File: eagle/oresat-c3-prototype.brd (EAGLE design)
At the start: 99.8 x 94.7 mm, 107 parts, among them J1 J-SAMTEC-TFM-110-X1-XXX-D-RA, J10 2X8X1.27, J11 2X8X1.27, J12 2X8X1.27, J2 U.FL, J3 U.FL, J4 U.FL, J6 J-SAMTEC-TFM-120-X1-XXX-D-RA, J7 FTSH-105-XX-X-DV-K, J8 SD_CARD_SOCKET, J9 2X8X1.27, Q1 MOSFET-PCH-SOT23-6, U1 MAX892LEUA+T, U2 TCAN330, U3 TCAN330, U4 TPS259621 - eFuse, U5 TPS62111RSA, U6 MAX6373KA+21-0078H-L, U7 STM32F446RE, X1 16MHZ-2.5x2mm

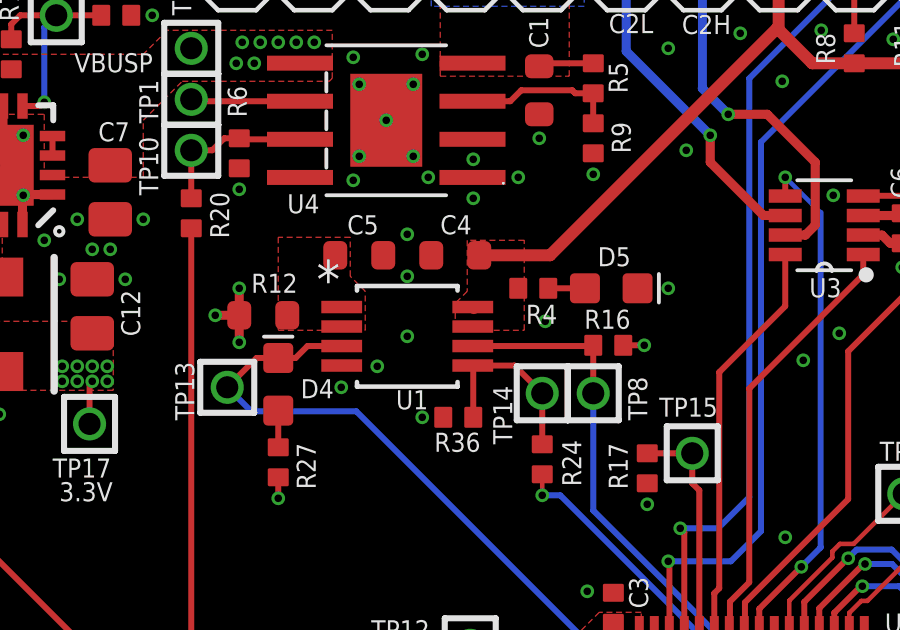
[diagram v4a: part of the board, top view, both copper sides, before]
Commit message: Replaced new ICs with versions in the oresat-eagle-libraries repo
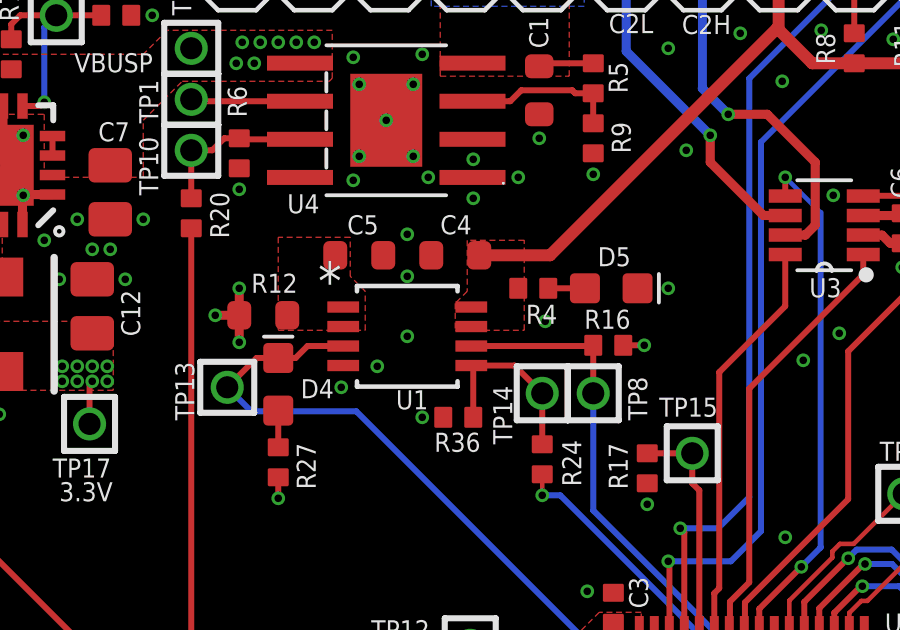
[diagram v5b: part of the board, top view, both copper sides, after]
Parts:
- U1: value MAX892LEUA+T -> MAX892LEUA+T21-0036K-L; device Robins_Parts:21-0036K -> U-Maxim-MAX892LEUA+T-power-switch:21-0036K-L
- U4: device Robins_Parts:SO-POWERPAD-8 -> U-TI-TPS2596XX-eFuse:SO-POWERPAD-8
- U6: value MAX6373KA+21-0078H-L -> MAX6374KA-T21-0078H-L; device MAXIM:21-0078H-L -> U-Maxim-MAX6374-watchdog:21-0078H-L
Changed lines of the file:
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@@
 <attribute name="VALUE" x="61.905" y="75.565" size="1.27" layer="27" rot="R90"/>
 </element>
-<element name="U6" library="MAXIM" package="21-0078H-L" value="MAX6373KA+21-0078H-L" x="15.11" y="72.69" smashed="yes">
-<attribute name="MANUFACTURER_PART_NUMBER" value="MAX6374KA+" x="15.11" y="72.69" size="1.778" layer="27" display="off"/>
+<element name="U6" library="U-Maxim-MAX6374-watchdog" package="21-0078H-L" value="MAX6374KA-T21-0078H-L" x="15.11" y="72.69" smashed="yes">
+<attribute name="MANUFACTURER_PART_NUMBER" value="max6374kat" x="15.11" y="72.69" size="1.778" layer="27" display="off"/>
 <attribute name="NAME" x="14.5334" y="70.155" size="0.635" layer="25" font="vector" ratio="20" rot="SR0"/>
 <attribute name="VENDOR" value="Maxim Integrated Products" x="15.11" y="72.69" size="1.778" layer="27" display="off"/>
@@
 <attribute name="VALUE" x="21.397" y="75.184" size="0.4064" layer="27" rot="R90"/>
 </element>
-<element name="U4" library="Robins_Parts" package="SO-POWERPAD-8" value="TPS259621 - eFuse" x="41.8" y="73.8" smashed="yes" rot="R90">
+<element name="U4" library="U-TI-TPS2596XX-eFuse" package="SO-POWERPAD-8" value="TPS259621 - eFuse" x="41.8" y="73.8" smashed="yes" rot="R90">
 <attribute name="NAME" x="38.5" y="70.7" size="0.635" layer="25" font="vector" ratio="20"/>
 <attribute name="VALUE" x="47.1594" y="70.5234" size="1.27" layer="27" rot="R90"/>
 </element>
-<element name="U1" library="Robins_Parts" package="21-0036K" value="MAX892LEUA+T" x="42.5" y="66.6" smashed="yes">
+<element name="U1" library="U-Maxim-MAX892LEUA+T-power-switch" package="21-0036K-L" value="MAX892LEUA+T21-0036K-L" x="42.5" y="66.6" smashed="yes">
 <attribute name="MANUFACTURER_PART_NUMBER" value="MAX892LEUA+T" x="42.5" y="66.6" size="1.778" layer="27" display="off"/>
 <attribute name="NAME" x="42.1234" y="64.165" size="0.635" layer="25" font="vector" ratio="20" rot="SR0"/>
@@
 <contactref element="U1" pad="7"/>
 <contactref element="U1" pad="8"/>
-<wire x1="44.6844" y1="67.575" x2="44.7194" y2="67.54" width="0.4" layer="1"/>
 <wire x1="60" y1="75.7" x2="57.4" y2="75.7" width="0.4" layer="1"/>
 <wire x1="57.4" y1="75.7" x2="56" y2="75.7" width="0.4" layer="1"/>
@@
 <wire x1="55.735" y1="49.235" x2="55.8" y2="49.3" width="0.2" layer="1"/>
 <contactref element="D4" pad="C"/>
-<wire x1="40.3156" y1="66.275" x2="39.175" y2="66.275" width="0.2" layer="1"/>
+<wire x1="40.3656" y1="66.275" x2="39.175" y2="66.275" width="0.2" layer="1"/>
 <wire x1="38.777" y1="65.877" x2="38.2" y2="65.877" width="0.2" layer="1"/>
 <wire x1="39.175" y1="66.275" x2="38.777" y2="65.877" width="0.2" layer="1"/>
@@
 <wire x1="47" y1="64.7" x2="47" y2="63" width="0.2" layer="1"/>
 <contactref element="U1" pad="5"/>
-<wire x1="44.6844" y1="65.625" x2="46.075" y2="65.625" width="0.2" layer="1"/>
+<wire x1="44.6344" y1="65.625" x2="46.075" y2="65.625" width="0.2" layer="1"/>
 <wire x1="47" y1="64.7" x2="46.075" y2="65.625" width="0.2" layer="1"/>
 <wire x1="44.7" y1="63.9" x2="44.7" y2="65.6094" width="0.2" layer="1"/>
-<wire x1="44.7" y1="65.6094" x2="44.6844" y2="65.625" width="0.2" layer="1"/>
+<wire x1="44.7" y1="65.6094" x2="44.6344" y2="65.625" width="0.2" layer="1"/>
 </signal>
 <signal name="OPD_!FAULT">
@@
 <contactref element="U1" pad="6"/>
 <wire x1="48.675" y1="66.275" x2="48.7" y2="66.3" width="0.2" layer="1"/>
-<wire x1="44.6844" y1="66.275" x2="48.675" y2="66.275" width="0.2" layer="1"/>
+<wire x1="44.6344" y1="66.275" x2="48.675" y2="66.275" width="0.2" layer="1"/>
 <wire x1="48.7" y1="66.3" x2="48.7" y2="64.7" width="0.2" layer="1"/>
 <wire x1="48.7" y1="60.7940875" x2="48.7" y2="64.7" width="0.2" layer="16"/>
@@
 <contactref element="C5" pad="1"/>
 <contactref element="R12" pad="1"/>
+<contactref element="U1" pad="2"/>
 <contactref element="U1" pad="1"/>
-<contactref element="U1" pad="2"/>
 <polygon width="0.2" layer="1" isolate="0.2" thermals="no">
 <vertex x="41.1" y="66.8"/>

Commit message: replaced the SD Card socket with a part in the oresat libraries
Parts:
- J8: device SparkFun-Connectors:SD -> J-4UCON-SparkfunPN-PRT-12769-SD-MMC-card-socket:SD
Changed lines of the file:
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@@
 <attribute name="VALUE" x="57.1" y="72.2" size="0.635" layer="27" ratio="20" rot="R90"/>
 </element>
-<element name="J8" library="SparkFun-Connectors" library_urn="urn:adsk.eagle:library:513" package="SD" package3d_urn="urn:adsk.eagle:package:38262/1" value="SD_CARD_SOCKET" x="70" y="39.3" smashed="yes" rot="R270">
+<element name="J8" library="J-4UCON-SparkfunPN-PRT-12769-SD-MMC-card-socket" package="SD" value="SD_CARD_SOCKET" x="70" y="39.3" smashed="yes" rot="R270">
 <attribute name="NAME" x="85.2" y="38.8" size="0.635" layer="25" font="vector" ratio="20"/>
 <attribute name="PROD_ID" value="CONN-11976" x="70" y="39.3" size="1.778" layer="27" rot="R270" display="off"/>

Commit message: Last minute tsilk clean up; all looks good!
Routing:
- net GND: vias 205 -> 231
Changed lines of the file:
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@@
 <setting verticaltext="up"/>
 </settings>
-<grid distance="3" unitdist="mm" unit="mm" style="lines" multiple="1" display="yes" altdistance="0.005" altunitdist="mm" altunit="mm"/>
+<grid distance="0.1" unitdist="mm" unit="mm" style="lines" multiple="1" display="yes" altdistance="0.005" altunitdist="mm" altunit="mm"/>
 <layers>
 <layer number="1" name="Top" color="4" fill="1" visible="yes" active="yes"/>
@@
 <layer number="23" name="tOrigins" color="15" fill="1" visible="yes" active="yes"/>
 <layer number="24" name="bOrigins" color="15" fill="1" visible="no" active="yes"/>
-<layer number="25" name="tNames" color="7" fill="1" visible="no" active="yes"/>
+<layer number="25" name="tNames" color="7" fill="1" visible="yes" active="yes"/>
 <layer number="26" name="bNames" color="7" fill="1" visible="no" active="yes"/>
 <layer number="27" name="tValues" color="7" fill="1" visible="no" active="yes"/>
 <layer number="28" name="bValues" color="7" fill="1" visible="no" active="yes"/>
-<layer number="29" name="tStop" color="7" fill="3" visible="no" active="yes"/>
+<layer number="29" name="tStop" color="7" fill="3" visible="yes" active="yes"/>
 <layer number="30" name="bStop" color="7" fill="6" visible="no" active="yes"/>
 <layer number="31" name="tCream" color="7" fill="4" visible="no" active="yes"/>
@@
 <circle x="48" y="26" radius="2.236065625" width="0.1524" layer="21"/>
 <circle x="48" y="17" radius="2.236065625" width="0.1524" layer="21"/>
-<text x="19.7" y="11.8" size="0.635" layer="21" font="vector" ratio="20">NRST</text>
+<text x="24.2" y="11.9" size="0.635" layer="21" font="vector" ratio="20">NRST</text>
 <text x="25.6" y="48.2" size="0.635" layer="21" font="vector" ratio="20">1</text>
 <text x="42" y="44.8" size="0.635" layer="21" font="vector" ratio="20">PA1</text>
@@
 <attribute name="MFR" value="ECS Inc." x="44.7" y="52.6" size="1.778" layer="27" rot="R270" display="off"/>
 <attribute name="MPN" value="ECS-160-10-36Q-ES-TR" x="44.7" y="52.6" size="1.778" layer="27" rot="R270" display="off"/>
-<attribute name="NAME" x="42.628" y="54.132" size="0.635" layer="25" font="vector" ratio="20" rot="R270"/>
+<attribute name="NAME" x="42.3" y="52.3" size="0.635" layer="25" font="vector" ratio="20"/>
 <attribute name="VALUE" x="44.691" y="52.605" size="0.5" layer="27" ratio="20" rot="R270" align="center"/>
 </element>
@@
 </element>
 <element name="TP2" library="Tova" package="2MM-TEST-POINT" value="TEST-POINT" x="23" y="12.5" smashed="yes">
-<attribute name="NAME" x="25" y="12.2" size="0.635" layer="25" font="vector" ratio="20"/>
+<attribute name="NAME" x="24.1" y="12.8" size="0.635" layer="25" font="vector" ratio="20"/>
 </element>
 <element name="R24" library="oresat-rcl" package=".0402-B-NOSILK" value="10k" x="47" y="62.5" smashed="yes" rot="R270">
@@
 <via x="9" y="39" extent="1-16" drill="0.254"/>
 <via x="12" y="27" extent="1-16" drill="0.254"/>
+<via x="53.3" y="72.8" extent="1-16" drill="0.254"/>
+<via x="53.4" y="58.6" extent="1-16" drill="0.254"/>
+<via x="59.9" y="59.1" extent="1-16" drill="0.254"/>
+<via x="58.8" y="57.5" extent="1-16" drill="0.254"/>
+<via x="64.1" y="55.6" extent="1-16" drill="0.254"/>
+<via x="64.6" y="62.1" extent="1-16" drill="0.254"/>
+<via x="57.3" y="60.4" extent="1-16" drill="0.254"/>
+<via x="68" y="39.9" extent="1-16" drill="0.254"/>
+<via x="67" y="48.9" extent="1-16" drill="0.254"/>
+<via x="68.8" y="48.4" extent="1-16" drill="0.254"/>
+<via x="72" y="50.3" extent="1-16" drill="0.254"/>
+<via x="58.31" y="41.65" extent="1-16" drill="0.254"/>
+<via x="54.71" y="39.05" extent="1-16" drill="0.254"/>
+<via x="52.01" y="38.95" extent="1-16" drill="0.254"/>
+<via x="51.81" y="31.25" extent="1-16" drill="0.254"/>
+<via x="53.31" y="29.65" extent="1-16" drill="0.254"/>
+<via x="89" y="4.5" extent="1-16" drill="0.254"/>
+<via x="6" y="83" extent="1-16" drill="0.254"/>
+<via x="6" y="69" extent="1-16" drill="0.254"/>
+<via x="6" y="52" extent="1-16" drill="0.254"/>
+<via x="17.7" y="21.7" extent="1-16" drill="0.254"/>
+<via x="22.7" y="21.7" extent="1-16" drill="0.254"/>
+<via x="21.7" y="11.8" extent="1-16" drill="0.254"/>
+<via x="17.6" y="7.7" extent="1-16" drill="0.254"/>
+<via x="6.8" y="17.4" extent="1-16" drill="0.254"/>
+<via x="69" y="10" extent="1-16" drill="0.254"/>
 </signal>
 <signal name="SPI1_SCK">

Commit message: C3 Functional Description Folder
Contains images of all block diagrams and a document that describes the functionality of each subsystem on the C3 board.
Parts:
- D3: value RED -> GREEN
- D4: value AMBER -> GREEN
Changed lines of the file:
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@@
 <?xml version="1.0" encoding="utf-8"?>
 <!DOCTYPE eagle SYSTEM "eagle.dtd">
-<eagle version="9.5.1">
+<eagle version="9.5.2">
 <drawing>
 <settings>
@@
 <element name="JP5" library="pinhead" library_urn="urn:adsk.eagle:library:325" package="1X05" package3d_urn="urn:adsk.eagle:package:22469/2" value="" x="13.5" y="53.6" smashed="yes" rot="R270">
 <attribute name="NAME" x="12.6" y="60.3" size="0.635" layer="25" font="vector" ratio="20"/>
+<attribute name="POPULARITY" value="69" x="13.5" y="53.6" size="1.778" layer="27" rot="R270" display="off"/>
 <attribute name="VALUE" x="10.325" y="59.95" size="1.27" layer="27" rot="R270"/>
 </element>
@@
 <attribute name="VALUE" x="19" y="12.65" size="0.8" layer="27" font="vector" ratio="15"/>
 </element>
-<element name="D3" library="SparkFun-LED" library_urn="urn:adsk.eagle:library:529" package="LED-0603" package3d_urn="urn:adsk.eagle:package:39354/1" value="RED" x="12.4" y="70.5" smashed="yes" rot="R270">
+<element name="D3" library="SparkFun-LED" library_urn="urn:adsk.eagle:library:529" package="LED-0603" package3d_urn="urn:adsk.eagle:package:39354/1" value="GREEN" x="12.4" y="70.5" smashed="yes" rot="R270">
 <attribute name="NAME" x="11.135" y="70.6" size="0.635" layer="25" font="vector" ratio="20" rot="R270" align="bottom-center"/>
 <attribute name="PROD_ID" value="DIO-00821" x="16" y="70.2" size="0.635" layer="27" font="vector" ratio="20" rot="R270" display="off"/>
@@
 <element name="JP8" library="pinhead" library_urn="urn:adsk.eagle:library:325" package="1X02" package3d_urn="urn:adsk.eagle:package:22435/2" value="" x="19" y="25.5" smashed="yes" rot="R180">
 <attribute name="NAME" x="18.1838" y="27.2288" size="0.635" layer="25" font="vector" ratio="20"/>
+<attribute name="POPULARITY" value="98" x="19" y="25.5" size="1.778" layer="27" rot="R180" display="off"/>
 <attribute name="VALUE" x="21.54" y="28.675" size="1.27" layer="27" rot="R180"/>
 </element>
@@
 <element name="JP9" library="pinhead" library_urn="urn:adsk.eagle:library:325" package="1X10" package3d_urn="urn:adsk.eagle:package:22406/2" value="" x="22" y="82.8" smashed="yes" rot="R180">
 <attribute name="NAME" x="8.9212" y="82.0738" size="0.635" layer="25" font="vector" ratio="20" rot="R90"/>
+<attribute name="POPULARITY" value="35" x="22" y="82.8" size="1.778" layer="27" rot="R180" display="off"/>
 <attribute name="VALUE" x="34.7" y="85.975" size="1.27" layer="27" rot="R180"/>
 </element>
 <element name="JP10" library="pinhead" library_urn="urn:adsk.eagle:library:325" package="2X05" package3d_urn="urn:adsk.eagle:package:22470/2" value="" x="41.91" y="80.01" smashed="yes" rot="R180">
 <attribute name="NAME" x="41" y="83" size="0.635" layer="25" font="vector" ratio="20"/>
+<attribute name="POPULARITY" value="35" x="41.91" y="80.01" size="1.778" layer="27" rot="R180" display="off"/>
 <attribute name="VALUE" x="48.26" y="84.455" size="1.27" layer="27" rot="R180"/>
 </element>
@@
 <element name="JP3" library="pinhead" library_urn="urn:adsk.eagle:library:325" package="1X03" package3d_urn="urn:adsk.eagle:package:22458/2" value="" x="13.5" y="42.3" smashed="yes" rot="R90">
 <attribute name="NAME" x="12.6" y="46.7" size="0.635" layer="25" font="vector" ratio="20"/>
+<attribute name="POPULARITY" value="92" x="13.5" y="42.3" size="1.778" layer="27" rot="R90" display="off"/>
 <attribute name="VALUE" x="16.675" y="38.49" size="1.27" layer="27" rot="R90"/>
 </element>
@@
 <attribute name="VALUE" x="39.7" y="67.7" size="0.8" layer="27" font="vector" ratio="15"/>
 </element>
-<element name="D4" library="SparkFun-LED" library_urn="urn:adsk.eagle:library:529" package="LED-0603" package3d_urn="urn:adsk.eagle:package:39354/1" value="AMBER" x="38.2" y="65" smashed="yes" rot="R90">
+<element name="D4" library="SparkFun-LED" library_urn="urn:adsk.eagle:library:529" package="LED-0603" package3d_urn="urn:adsk.eagle:package:39354/1" value="GREEN" x="38.2" y="65" smashed="yes" rot="R90">
 <attribute name="NAME" x="39.5" y="64.535" size="0.635" layer="25" font="vector" ratio="20" align="bottom-center"/>
 <attribute name="PROD_ID" value="" x="34.7" y="65.3" size="0.635" layer="27" ratio="20" rot="R90" display="off"/>
@@
 <element name="JP2" library="pinhead" library_urn="urn:adsk.eagle:library:325" package="2X05" package3d_urn="urn:adsk.eagle:package:22470/2" value="" x="65.66" y="80.25" smashed="yes" rot="R270">
 <attribute name="NAME" x="64.74" y="72.995" size="0.635" layer="25" font="vector" ratio="20"/>
+<attribute name="POPULARITY" value="35" x="65.66" y="80.25" size="1.778" layer="27" rot="R270" display="off"/>
 <attribute name="VALUE" x="61.215" y="86.6" size="1.27" layer="27" rot="R270"/>
 </element>
@@
 <element name="JP1" library="pinhead" library_urn="urn:adsk.eagle:library:325" package="2X05" package3d_urn="urn:adsk.eagle:package:22470/2" value="" x="54.88" y="80.01" smashed="yes" rot="R180">
 <attribute name="NAME" x="54.07" y="82.865" size="0.635" layer="25" font="vector" ratio="20"/>
+<attribute name="POPULARITY" value="35" x="54.88" y="80.01" size="1.778" layer="27" rot="R180" display="off"/>
 <attribute name="VALUE" x="61.23" y="84.455" size="1.27" layer="27" rot="R180"/>
 </element>
@@
 <element name="JP11" library="pinhead" library_urn="urn:adsk.eagle:library:325" package="2X05" package3d_urn="urn:adsk.eagle:package:22470/2" value="" x="22.5" y="53.65" smashed="yes" rot="R90">
 <attribute name="NAME" x="21.6" y="46.175" size="0.635" layer="25" font="vector" ratio="20"/>
+<attribute name="POPULARITY" value="35" x="22.5" y="53.65" size="1.778" layer="27" rot="R90" display="off"/>
 <attribute name="VALUE" x="26.945" y="47.3" size="1.27" layer="27" rot="R90"/>
 </element>
